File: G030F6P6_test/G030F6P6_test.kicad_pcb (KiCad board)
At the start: 2 copper layers, 3 parts, among them J1 Conn_01x10_Female, J2 Conn_01x10_Female, U1 STM32G030FxP

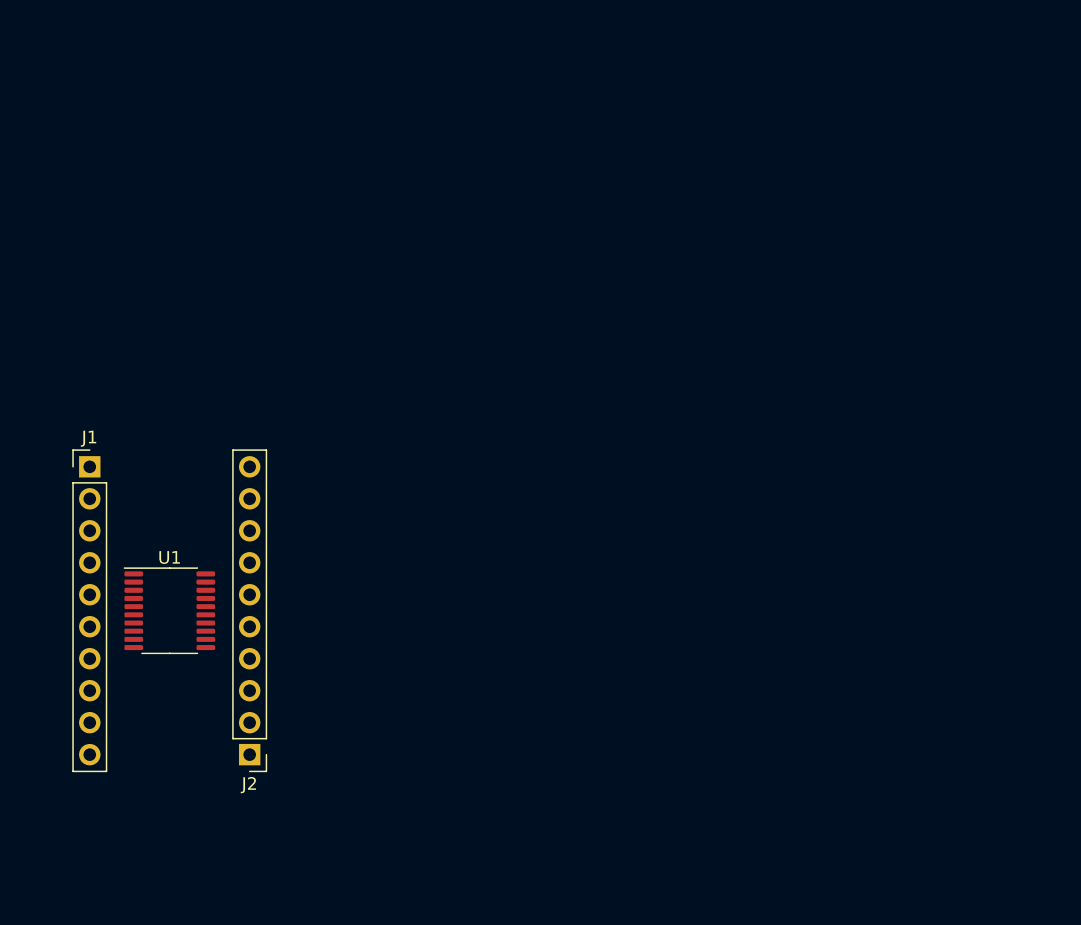
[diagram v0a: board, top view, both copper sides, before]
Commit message: Update G030F6P6_test.kicad_pcb
元件初次放置
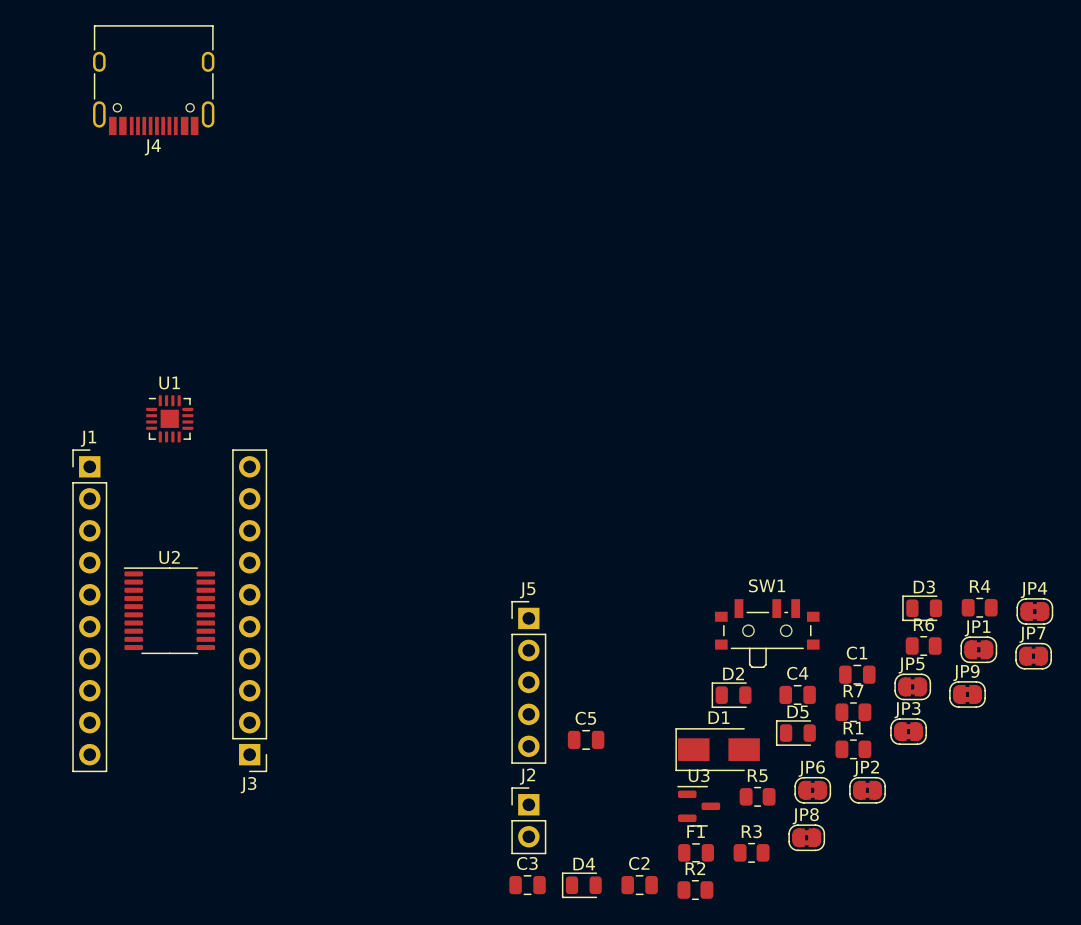
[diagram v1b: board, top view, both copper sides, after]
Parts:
- added C1: 0.1uF, Capacitor_SMD:C_0805_2012Metric, F.Cu at (185.4, 90.2)
- added C2: 0.1uF, Capacitor_SMD:C_0805_2012Metric, F.Cu at (168.1, 106.9)
- added C3: 0.1uF, Capacitor_SMD:C_0805_2012Metric, F.Cu at (159.2, 106.9)
- added C4: 0.1uF, Capacitor_SMD:C_0805_2012Metric, F.Cu at (180.7, 91.8)
- added C5: 0.1uF, Capacitor_SMD:C_0805_2012Metric, F.Cu at (163.9, 95.3)
- added D1: D_Schottky, Diode_SMD:D_SMA, F.Cu at (174.4, 96.1)
- added D2: PWR, LED_SMD:LED_0805_2012Metric, F.Cu at (175.6, 91.8)
- added D3: RX, LED_SMD:LED_0805_2012Metric, F.Cu at (190.7, 84.9)
- added D4: TX, LED_SMD:LED_0805_2012Metric, F.Cu at (163.7, 106.9)
- added D5: ACT#, LED_SMD:LED_0805_2012Metric, F.Cu at (180.7, 94.8)
- added F1: Fuse, Fuse:Fuse_0805_2012Metric, F.Cu at (172.6, 104.3)
- added J2: Conn_01x02_Male, Connector_PinHeader_2.54mm:PinHeader_1x02_P2.54mm_Vertical, F.Cu at (159.3, 100.5)
- added J4: USB_C_Receptacle_USB2.0, Connector_USB:USB_C_Receptacle_HRO_TYPE-C-31-M-12, F.Cu at (129.5, 42.5)
- added J5: Conn_01x05_Female, Connector_PinHeader_2.54mm:PinHeader_1x05_P2.54mm_Vertical, F.Cu at (159.3, 85.7)
- added JP1: SolderJumper_2_Bridged, Jumper:SolderJumper-2_P1.3mm_Bridged2Bar_RoundedPad1.0x1.5mm, F.Cu at (195.1, 88.2)
- added JP2: SolderJumper_2_Bridged, Jumper:SolderJumper-2_P1.3mm_Bridged2Bar_RoundedPad1.0x1.5mm, F.Cu at (186.2, 99.3)
- added JP3: SolderJumper_2_Bridged, Jumper:SolderJumper-2_P1.3mm_Bridged2Bar_RoundedPad1.0x1.5mm, F.Cu at (189.5, 94.7)
- added JP4: SolderJumper_2_Bridged, Jumper:SolderJumper-2_P1.3mm_Bridged2Bar_RoundedPad1.0x1.5mm, F.Cu at (199.5, 85.2)
- added JP5: SolderJumper_2_Bridged, Jumper:SolderJumper-2_P1.3mm_Bridged2Bar_RoundedPad1.0x1.5mm, F.Cu at (189.8, 91.1)
- added JP6: SolderJumper_2_Bridged, Jumper:SolderJumper-2_P1.3mm_Bridged2Bar_RoundedPad1.0x1.5mm, F.Cu at (181.9, 99.3)
- added JP7: SolderJumper_2_Bridged, Jumper:SolderJumper-2_P1.3mm_Bridged2Bar_RoundedPad1.0x1.5mm, F.Cu at (199.4, 88.7)
- added JP8: SolderJumper_2_Bridged, Jumper:SolderJumper-2_P1.3mm_Bridged2Bar_RoundedPad1.0x1.5mm, F.Cu at (181.4, 103.1)
- added JP9: SolderJumper_2_Bridged, Jumper:SolderJumper-2_P1.3mm_Bridged2Bar_RoundedPad1.0x1.5mm, F.Cu at (194.2, 91.7)
- added R1: 100K, Resistor_SMD:R_0805_2012Metric, F.Cu at (185.1, 96.1)
- added R2: 5K1, Resistor_SMD:R_0805_2012Metric, F.Cu at (172.6, 107.3)
- added R3: 5K1, Resistor_SMD:R_0805_2012Metric, F.Cu at (177.0, 104.3)
- added R4: 330, Resistor_SMD:R_0805_2012Metric, F.Cu at (195.1, 84.8)
- added R5: 1k, Resistor_SMD:R_0805_2012Metric, F.Cu at (177.5, 99.9)
- added R6: 1k, Resistor_SMD:R_0805_2012Metric, F.Cu at (190.7, 87.9)
- added R7: 1k, Resistor_SMD:R_0805_2012Metric, F.Cu at (185.1, 93.2)
- added SW1: SW_Push_SPDT, Button_Switch_SMD:SW_SPDT_PCM12, F.Cu at (178.3, 86.3)
- added U1: CH343P, Package_DFN_QFN:QFN-16-1EP_3x3mm_P0.5mm_EP1.45x1.45mm, F.Cu at (130.8, 69.8)
- added U3: XC6206P332MR, Package_TO_SOT_SMD:SOT-23, F.Cu at (172.8, 100.6)
- renumbered J2 to J3, U1 to U2

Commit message: PCB 板放置零件
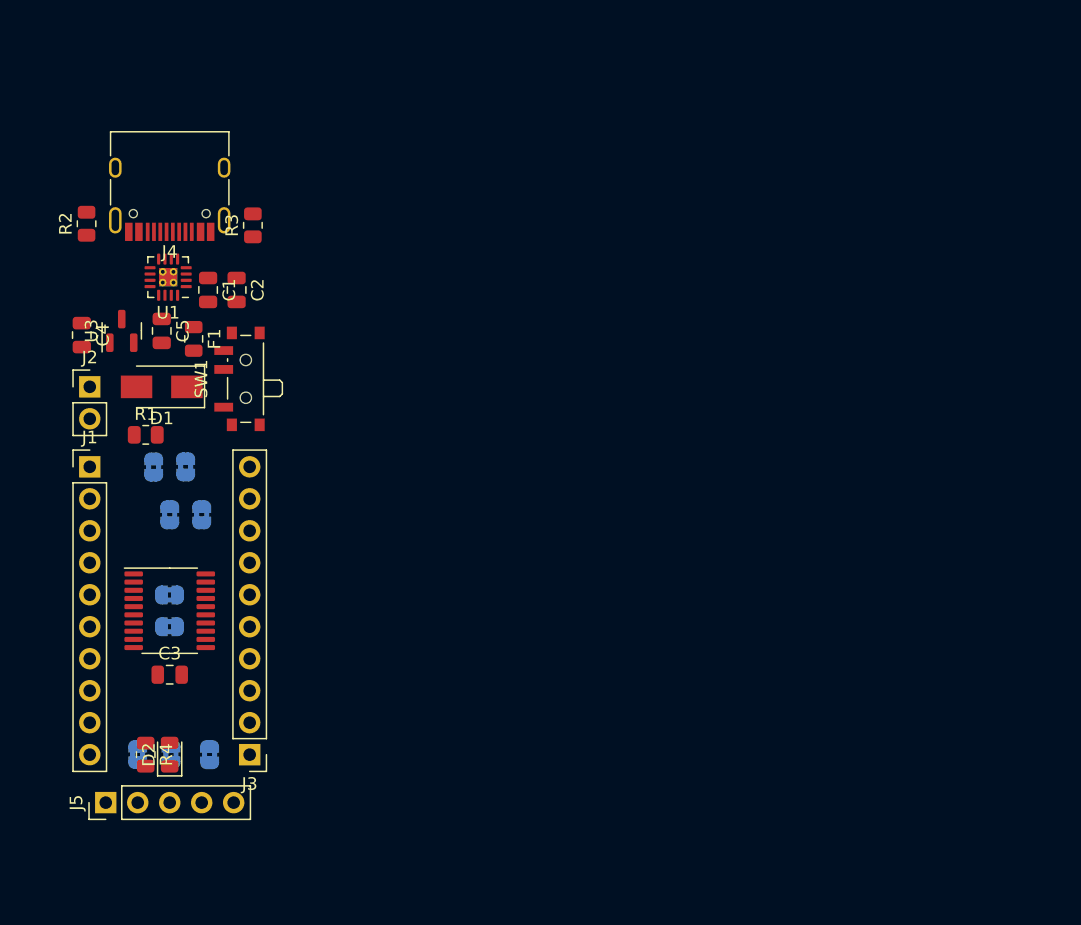
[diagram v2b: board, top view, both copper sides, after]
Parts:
- removed D3: RX, LED_SMD:LED_0805_2012Metric
- removed D4: TX, LED_SMD:LED_0805_2012Metric
- removed D5: ACT#, LED_SMD:LED_0805_2012Metric
- removed R5, R6, R7: 1k, Resistor_SMD:R_0805_2012Metric
- JP1, JP2, JP3, JP4, JP5, JP6, JP7, JP8, JP9: moved to B.Cu
- U1: footprint Package_DFN_QFN:QFN-16-1EP_3x3mm_P0.5mm_EP1.45x1.45mm -> Package_DFN_QFN:QFN-16-1EP_3x3mm_P0.5mm_EP1.45x1.45mm_ThermalVias
- moved R2 71.7 mm to (124.2, 54.4), turned to 90 degrees
- moved JP7 71.6 mm to (128.3, 96.5), turned to 90 degrees
- moved JP4 70.9 mm to (129.5, 73.7), turned to -90 degrees
- moved R4 67.3 mm to (128.9, 96.5), turned to -90 degrees
- moved R3 63.7 mm to (137.4, 54.5), turned to 90 degrees
- moved C4 63.6 mm to (123.8, 63.2), turned to -90 degrees
- moved JP1 62.6 mm to (133.3, 77.5), turned to -90 degrees
- moved R1 61.5 mm to (128.9, 71.1)
- moved JP3 61.1 mm to (132.1, 73.7), turned to -90 degrees
- moved JP9 60.4 mm to (134.0, 96.5), turned to 90 degrees
- moved C1 59.9 mm to (133.9, 59.6), turned to -90 degrees
- moved JP2 59.6 mm to (130.8, 77.5), turned to -90 degrees
- moved U3 59.4 mm to (127.0, 62.9), turned to 90 degrees
- moved JP5 59.2 mm to (130.8, 86.4)
- moved C2 57.1 mm to (136.1, 59.6), turned to -90 degrees
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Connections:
- R4 pad 2: +5V -> +3V3

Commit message: 畫線
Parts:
- moved JP9 2.96 mm to (133.5, 93.6)
- moved JP7 2.91 mm to (128.1, 93.6)
- moved JP8 2.89 mm to (130.8, 93.6)
- moved J4 1.93 mm to (130.8, 49.0)
- moved R2 1.93 mm to (124.2, 52.4)
- moved R3 1.93 mm to (137.4, 52.6)
- moved C1 1.59 mm to (134.7, 58.3)
- moved C2 1.47 mm to (136.8, 58.3)
- moved U1 0.91 mm to (131.3, 57.9)
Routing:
- net Net-(C2-Pad1): track 0.00 -> 7.48 mm
- net /USBD-: track 0.00 -> 5.49 mm
- net /USBD+: track 0.00 -> 5.46 mm, vias 0 -> 2
- net +5V: track 0.00 -> 3.31 mm
- net +3V3: track 0.00 -> 2.58 mm
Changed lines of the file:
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@@
   )
   (setup
+    (stackup
+      (layer "F.SilkS" (type "Top Silk Screen"))
+      (layer "F.Paste" (type "Top Solder Paste"))
+      (layer "F.Mask" (type "Top Solder Mask") (thickness 0.01))
+      (layer "F.Cu" (type "copper") (thickness 0.035))
+      (layer "dielectric 1" (type "core") (thickness 1.51) (material "FR4") (epsilon_r 4.5) (loss_tangent 0.02))
+      (layer "B.Cu" (type "copper") (thickness 0.035))
+      (layer "B.Mask" (type "Bottom Solder Mask") (thickness 0.01))
+      (layer "B.Paste" (type "Bottom Solder Paste"))
+      (layer "B.SilkS" (type "Bottom Silk Screen"))
+      (copper_finish "None")
+      (dielectric_constraints no)
+    )
     (pad_to_mask_clearance 0)
     (pcbplotparams
@@
   )
   (footprint "Resistor_SMD:R_0805_2012Metric" (layer "F.Cu")
-    (at 137.414 54.483 90)
+    (at 137.414 52.5526 90)
     (descr "Resistor SMD 0805 (2012 Metric), square (rectangular) end terminal, IPC_7351 nominal, (Body size source: IPC-SM-782 page 72, https://www.pcb-3d.com/wordpress/wp-content/uploads/ipc-sm-782a_amendment_1_and_2.pdf), generated with kicad-footprint-generator")
     (tags "resistor")
@@
   )
   (footprint "Capacitor_SMD:C_0805_2012Metric" (layer "F.Cu")
-    (at 133.858 59.6138 -90)
+    (at 134.747 58.293 -90)
     (descr "Capacitor SMD 0805 (2012 Metric), square (rectangular) end terminal, IPC_7351 nominal, (Body size source: IPC-SM-782 page 76, https://www.pcb-3d.com/wordpress/wp-content/uploads/ipc-sm-782a_amendment_1_and_2.pdf, https://docs.google.com/spreadsheets/d/1BsfQQcO9C6DZCsRaXUlFlo91Tg2WpOkGARC1WS5S8t0/edit?usp=sharing), generated with kicad-footprint-generator")
     (tags "capacitor")
@@
   )
   (footprint "Package_DFN_QFN:QFN-16-1EP_3x3mm_P0.5mm_EP1.45x1.45mm_ThermalVias" (layer "F.Cu")
-    (at 130.683 58.5978 180)
+    (at 131.2775 57.908 180)
     (descr "QFN, 16 Pin (http://cds.linear.com/docs/en/datasheet/37551fd.pdf), generated with kicad-footprint-generator ipc_noLead_generator.py")
     (tags "QFN NoLead")
@@
     (property "Sheetname" "")
     (attr smd)
-    (fp_text reference "U1" (at 0 -2.82 180) (layer "F.SilkS")
-      (effects (font (size 1 1) (thickness 0.15)))
-    )
-    (fp_text value "CH343P" (at 0 2.82 180) (layer "F.Fab")
-      (effects (font (size 1 1) (thickness 0.15)))
-    )
-    (fp_text user "${REFERENCE}" (at 0 0 180) (layer "F.Fab")
+    (fp_text reference "U1" (at 0 -2.82) (layer "F.SilkS")
+      (effects (font (size 1 1) (thickness 0.15)))
+    )
+    (fp_text value "CH343P" (at 0 2.82) (layer "F.Fab")
+      (effects (font (size 1 1) (thickness 0.15)))
+    )
+    (fp_text user "${REFERENCE}" (at 0 0) (layer "F.Fab")
       (effects (font (size 0.75 0.75) (thickness 0.11)))
     )
@@
   )
   (footprint "Connector_USB:USB_C_Receptacle_HRO_TYPE-C-31-M-12" (layer "F.Cu")
-    (at 130.81 50.9524 180)
+    (at 130.81 49.022 180)
     (descr "USB Type-C receptacle for USB 2.0 and PD, http://www.krhro.com/uploads/soft/180320/1-1P320120243.pdf")
     (tags "usb usb-c 2.0 pd")
@@
   )
   (footprint "Capacitor_SMD:C_0805_2012Metric" (layer "F.Cu")
-    (at 136.123 59.6138 -90)
+    (at 136.779 58.293 -90)
     (descr "Capacitor SMD 0805 (2012 Metric), square (rectangular) end terminal, IPC_7351 nominal, (Body size source: IPC-SM-782 page 76, https://www.pcb-3d.com/wordpress/wp-content/uploads/ipc-sm-782a_amendment_1_and_2.pdf, https://docs.google.com/spreadsheets/d/1BsfQQcO9C6DZCsRaXUlFlo91Tg2WpOkGARC1WS5S8t0/edit?usp=sharing), generated with kicad-footprint-generator")
     (tags "capacitor")
@@
   )
   (footprint "Resistor_SMD:R_0805_2012Metric" (layer "F.Cu")
-    (at 124.206 54.356 90)
+    (at 124.206 52.4256 90)
     (descr "Resistor SMD 0805 (2012 Metric), square (rectangular) end terminal, IPC_7351 nominal, (Body size source: IPC-SM-782 page 72, https://www.pcb-3d.com/wordpress/wp-content/uploads/ipc-sm-782a_amendment_1_and_2.pdf), generated with kicad-footprint-generator")
     (tags "resistor")
@@
   )
   (footprint "Jumper:SolderJumper-2_P1.3mm_Bridged2Bar_RoundedPad1.0x1.5mm" (layer "B.Cu")
-    (at 128.265 96.505 90)
+    (at 128.143 93.599 90)
     (descr "SMD Solder Jumper, 1x1.5mm, rounded Pads, 0.3mm gap, bridged with 2 copper strips")
     (tags "net tie solder jumper bridged")
@@
   )
   (footprint "Jumper:SolderJumper-2_P1.3mm_Bridged2Bar_RoundedPad1.0x1.5mm" (layer "B.Cu")
-    (at 133.98 96.52 90)
+    (at 133.477 93.599 90)
     (descr "SMD Solder Jumper, 1x1.5mm, rounded Pads, 0.3mm gap, bridged with 2 copper strips")
     (tags "net tie solder jumper bridged")
@@
       ))
   )
-  (footprint "Jumper:SolderJumper-2_P1.3mm_Bridged2Bar_RoundedPad1.0x1.5mm" (layer "B.Cu")
-    (at 130.905 96.505 90)
+  (footprint "Jumper:SolderJumper-2_P1.3mm_Bridged2Bar_RoundedPad1.0x1.5mm" locked (layer "B.Cu")
+    (at 130.81 93.614 90)
     (descr "SMD Solder Jumper, 1x1.5mm, rounded Pads, 0.3mm gap, bridged with 2 copper strips")
     (tags "net tie solder jumper bridged")
@@
     (fp_line (start -1.65 1.25) (end 1.65 1.25) (layer "B.CrtYd") (width 0.05))
     (fp_line (start 1.65 -1.25) (end -1.65 -1.25) (layer "B.CrtYd") (width 0.05))
-    (pad "1" smd custom (at -0.65 0 90) (size 1 0.5) (layers "B.Cu" "B.Mask")
+    (pad "1" smd custom locked (at -0.65 0 90) (size 1 0.5) (layers "B.Cu" "B.Mask")
       (net 40 "/SWCLK") (pinfunction "A") (pintype "passive") (zone_connect 2)
       (options (clearance outline) (anchor rect))
@@
           ) (width 0) (fill yes))
       ))
-    (pad "2" smd custom (at 0.65 0 90) (size 1 0.5) (layers "B.Cu" "B.Mask")
+    (pad "2" smd custom locked (at 0.65 0 90) (size 1 0.5) (layers "B.Cu" "B.Mask")
       (net 19 "/PIN19") (pinfunction "B") (pintype "passive") (zone_connect 2)
       (options (clearance outline) (anchor rect))
@@
       ))
   )
+  (segment (start 134.747 57.343) (end 134.681 57.343) (width 0.25) (layer "F.Cu") (net 21))
+  (segment (start 133.366 58.658) (end 132.715 58.658) (width 0.25) (layer "F.Cu") (net 21))
+  (segment (start 134.681 57.343) (end 133.366 58.658) (width 0.25) (layer "F.Cu") (net 21))
+  (segment (start 136.779 57.343) (end 136.779 56.261) (width 0.25) (layer "F.Cu") (net 23))
+  (segment (start 132.08 55.372) (end 131.5275 55.9245) (width 0.25) (layer "F.Cu") (net 23))
+  (segment (start 136.779 56.261) (end 135.89 55.372) (width 0.25) (layer "F.Cu") (net 23))
+  (segment (start 131.5275 55.9245) (end 131.5275 56.4705) (width 0.25) (layer "F.Cu") (net 23))
+  (segment (start 135.89 55.372) (end 132.08 55.372) (width 0.25) (layer "F.Cu") (net 23))
+  (segment (start 126.68 62.2475) (end 127 61.9275) (width 0.6) (layer "F.Cu") (net 24))
+  (segment (start 123.825 62.2475) (end 126.68 62.2475) (width 0.6) (layer "F.Cu") (net 24))
+  (segment (start 129.921 55.245) (end 129.794 55.245) (width 0.2) (layer "F.Cu") (net 34))
+  (segment (start 131.2595 55.059461) (end 131.0275 55.291461) (width 0.2) (layer "F.Cu") (net 34))
+  (segment (start 129.794 55.245) (end 130.06 54.979) (width 0.2) (layer "F.Cu") (net 34))
+  (segment (start 130.06 54.979) (end 130.06 53.067) (width 0.2) (layer "F.Cu") (net 34))
+  (segment (start 131.0275 55.291461) (end 131.0275 56.4705) (width 0.2) (layer "F.Cu") (net 34))
+  (via (at 131.2595 55.059461) (size 0.8) (drill 0.4) (layers "F.Cu" "B.Cu") (net 34))
+  (via (at 129.794 55.245) (size 0.8) (drill 0.4) (layers "F.Cu" "B.Cu") (net 34))
+  (segment (start 131.2595 55.059461) (end 131.073961 55.245) (width 0.2) (layer "B.Cu") (net 34))
+  (segment (start 131.073961 55.245) (end 129.794 55.245) (width 0.2) (layer "B.Cu") (net 34))
+  (segment (start 131.187 54.36) (end 130.56 54.36) (width 0.2) (layer "F.Cu") (net 35))
+  (segment (start 130.56 54.36) (end 130.56 53.067) (width 0.2) (layer "F.Cu") (net 35))
+  (segment (start 131.56 53.987) (end 131.187 54.36) (width 0.2) (layer "F.Cu") (net 35))
+  (segment (start 130.5275 56.4705) (end 130.56 56.438) (width 0.2) (layer "F.Cu") (net 35))
+  (segment (start 130.56 56.438) (end 130.56 54.36) (width 0.2) (layer "F.Cu") (net 35))
+  (segment (start 131.56 53.067) (end 131.56 53.987) (width 0.2) (layer "F.Cu") (net 35))
 )

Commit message: 布局完成
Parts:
- removed D1: D_Schottky, Diode_SMD:D_SMA
- removed J2: Conn_01x02_Male, Connector_PinHeader_2.54mm:PinHeader_1x02_P2.54mm_Vertical
- removed SW1: SW_Push_SPDT, Button_Switch_SMD:SW_SPDT_PCM12
- moved U3 12.4 mm to (130.9, 74.7)
- moved C4 12.4 mm to (127.8, 75.0)
- moved C5 12.4 mm to (133.9, 74.7)
- moved C2 11.6 mm to (138.0, 69.8)
- moved C1 11.6 mm to (136.0, 69.8)
- moved J4 11.6 mm to (130.8, 60.6)
- moved R3 11.6 mm to (137.4, 64.1)
- moved U1 11.6 mm to (131.3, 69.5)
- moved R2 11.6 mm to (124.2, 64.0)
- moved R1 8.64 mm to (128.7, 79.8), turned to 90 degrees
- moved JP4 7.37 mm to (132.8, 80.3)
- moved F1 7.01 mm to (127.6, 68.3)
- moved JP3 6.87 mm to (130.2, 80.3)
- moved JP7 5.99 mm to (134.1, 93.1)
- moved JP9 4.72 mm to (128.8, 93.1)
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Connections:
- C4 pad 1: +5V -> VBUS
- J5 pad 3: /SWDIO -> /SWCLK
- J5 pad 4: /SWCLK -> /SWDIO
- U1 pad 3: +5V -> VBUS
- U3 pad 3: +5V -> VBUS
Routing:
- net +3V3: track 2.58 -> 52.0 mm, vias 0 -> 1
- net /PIN19: track 0.00 -> 29.3 mm
- net /PIN18: track 0.00 -> 22.9 mm
- net /PIN6: track 0.00 -> 22.3 mm
- net /NRST: track 0.00 -> 21.7 mm
- net VBUS: track 0.00 -> 21.0 mm, vias 0 -> 2
- net /BOOT0: track 0.00 -> 17.9 mm, vias 0 -> 3
- net /PIN20: track 0.00 -> 17.2 mm
- net /PIN4: track 0.00 -> 17.1 mm, vias 0 -> 1
- net /PIN5: track 0.00 -> 15.8 mm, vias 0 -> 1
- net /TXD: track 0.00 -> 15.7 mm, vias 0 -> 1
- net /PIN1: track 0.00 -> 15.2 mm, vias 0 -> 1
- net /RXD: track 0.00 -> 14.8 mm, vias 0 -> 1
- net /PIN11: track 0.00 -> 11.4 mm
- net Net-(F1-Pad1): track 0.00 -> 10.8 mm, vias 0 -> 2
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- added copper zone on B.Cu, net GND
- added copper zone on F.Cu, net GND
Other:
- board outline added: 22.9 x 49.1 mm
- board text added: "BOT"
- board text added: "CLK"
- board text added: "DIO"
- board text added: "GND"
- board text added: "NRST"
- board text added: "PA0"
- board text added: "PA1"
- board text added: "PA11 PA9"
- board text added: "PA12 PA10"
- board text added: "PA13"
- board text added: "PA14 PA15"
- board text added: "PA2"
- board text added: "PA3"
- board text added: "PA4"
- board text added: "PA5"
- board text added: "PA6"
- board text added: "PA7"
- board text added: "PA8"
- board text added: "PB0 PB2"
- board text added: "PB3 PB6"
- board text added: "PB9 PC14"
- board text added: "PC15"
- board text added: "RST"
- board text added: "RXD"
- board text added: "STM32G030F6P6"
- board text added: "TXD"
- board text added: "VCC"
- board text added: "VDD"
- board text added: "~{RTS}"

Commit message: Update G030F6P6_test.kicad_pcb
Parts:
- added REF**: KiCad-Logo2_5mm_SilkScreen, Symbol:KiCad-Logo2_5mm_SilkScreen, B.Cu at (122.7, 63.0)
- moved F1 0.25 mm to (127.6, 68.6)
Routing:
- net Net-(F1-Pad1): track 10.8 -> 14.5 mm
